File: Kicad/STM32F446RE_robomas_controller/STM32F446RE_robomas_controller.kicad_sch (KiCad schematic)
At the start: 5 parts, among them U3 NUCLEO-F446RE

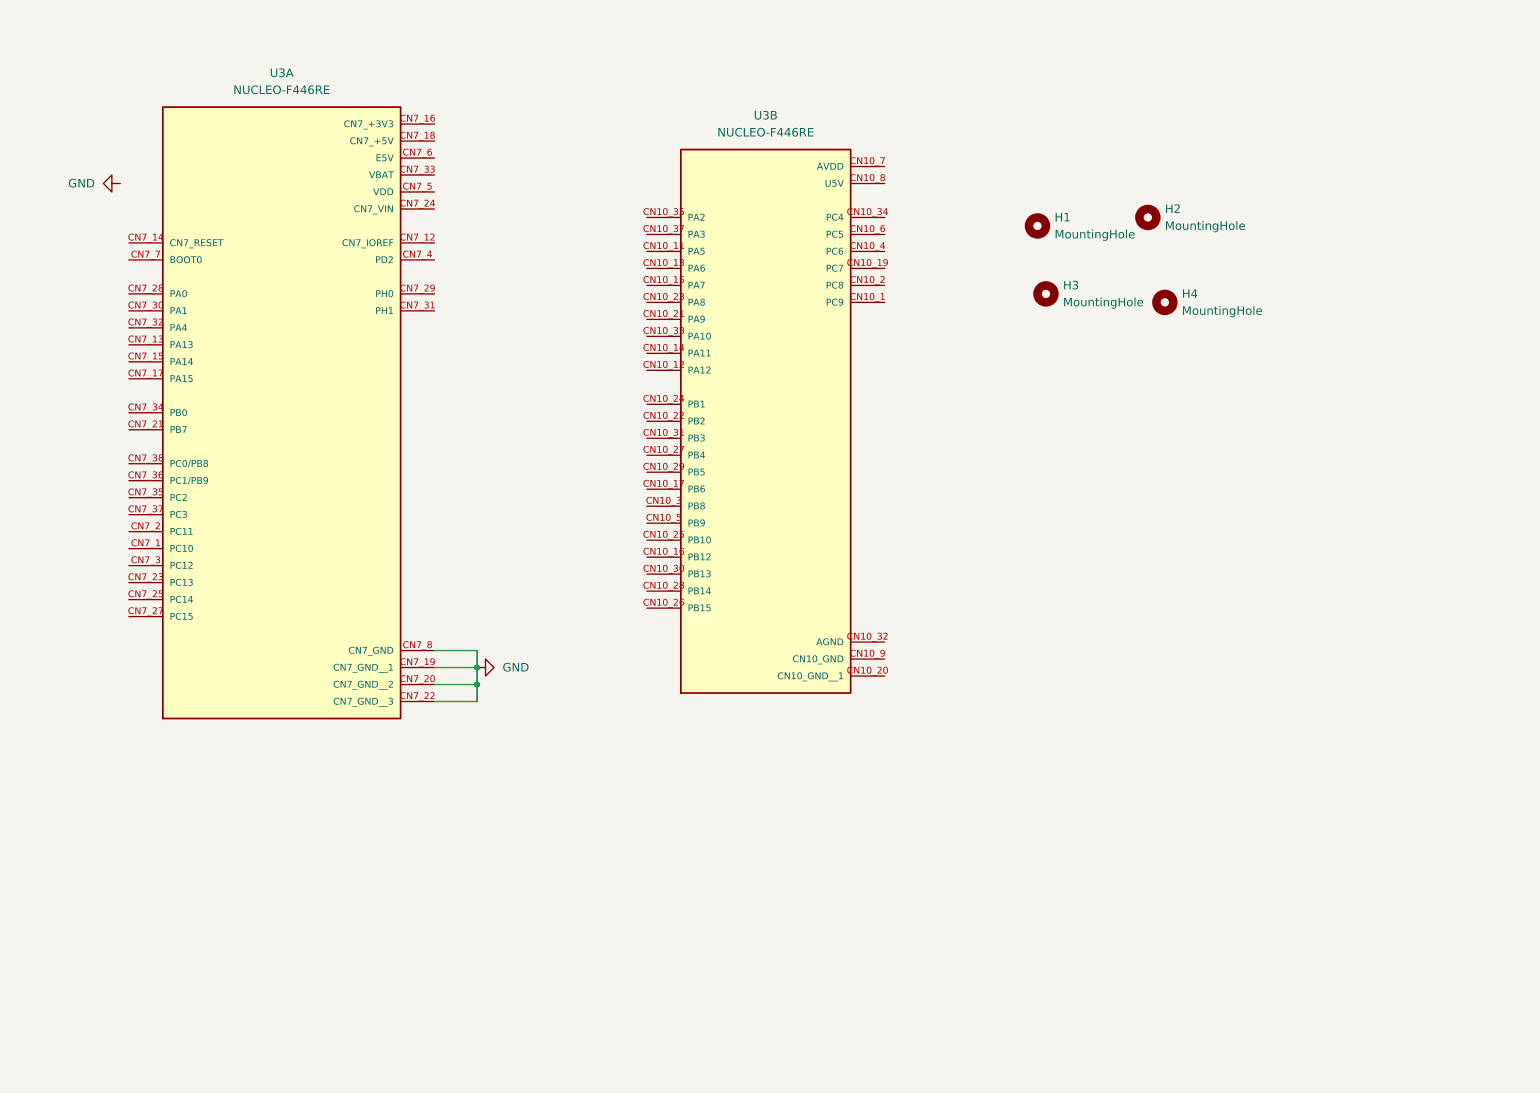
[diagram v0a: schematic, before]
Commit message: robomas用の回路完成
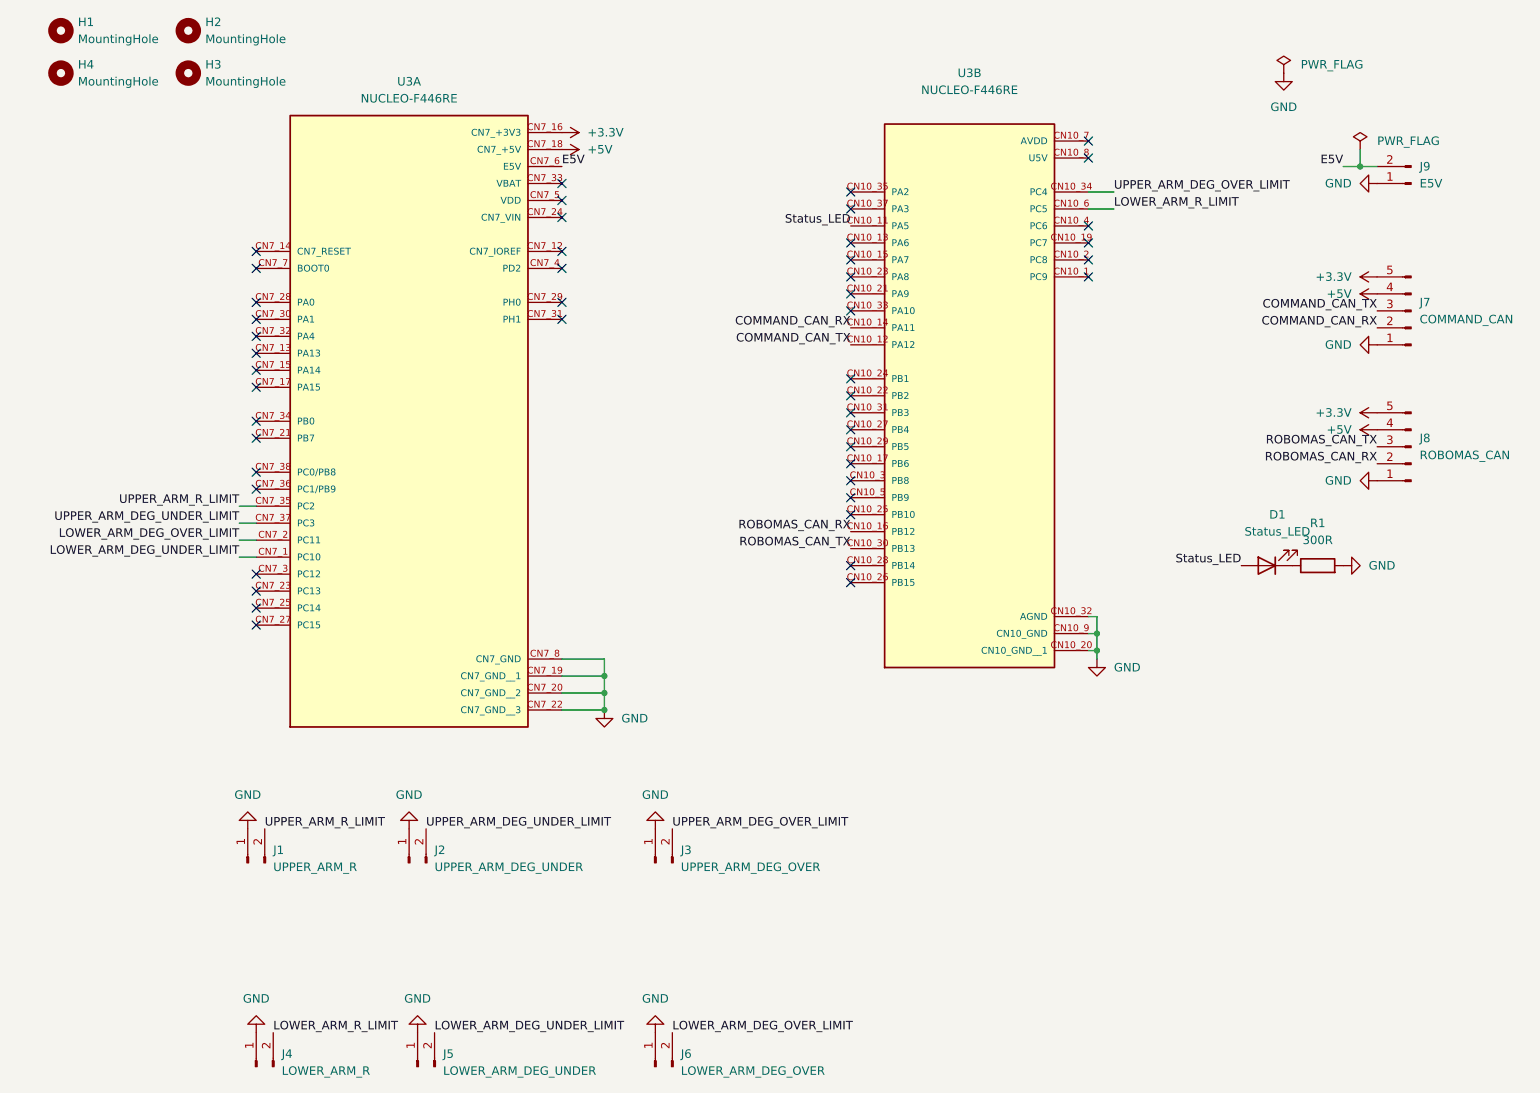
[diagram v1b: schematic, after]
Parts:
- added D1: Status_LED, LED_THT:LED_D3.0mm, symbol Device:LED
- added J1: UPPER_ARM_R, Connector_PinHeader_2.54mm:PinHeader_1x02_P2.54mm_Vertical, symbol Connector:Conn_01x02_Pin
- added J2: UPPER_ARM_DEG_UNDER, Connector_PinHeader_2.54mm:PinHeader_1x02_P2.54mm_Vertical, symbol Connector:Conn_01x02_Pin
- added J3: UPPER_ARM_DEG_OVER, Connector_PinHeader_2.54mm:PinHeader_1x02_P2.54mm_Vertical, symbol Connector:Conn_01x02_Pin
- added J4: LOWER_ARM_R, Connector_PinHeader_2.54mm:PinHeader_1x02_P2.54mm_Vertical, symbol Connector:Conn_01x02_Pin
- added J5: LOWER_ARM_DEG_UNDER, Connector_PinHeader_2.54mm:PinHeader_1x02_P2.54mm_Vertical, symbol Connector:Conn_01x02_Pin
- added J6: LOWER_ARM_DEG_OVER, Connector_PinHeader_2.54mm:PinHeader_1x02_P2.54mm_Vertical, symbol Connector:Conn_01x02_Pin
- added J7: COMMAND_CAN, Connector_PinHeader_2.54mm:PinHeader_1x05_P2.54mm_Vertical, symbol Connector:Conn_01x05_Pin
- added J8: ROBOMAS_CAN, Connector_PinHeader_2.54mm:PinHeader_1x05_P2.54mm_Vertical, symbol Connector:Conn_01x05_Pin
- added J9: E5V, Connector_PinHeader_2.54mm:PinHeader_1x02_P2.54mm_Vertical, symbol Connector:Conn_01x02_Pin
- added R1: 300R, Resistor_THT:R_Axial_DIN0207_L6.3mm_D2.5mm_P7.62mm_Horizontal, symbol Device:R
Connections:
- net GND: now also U3.CN10_20 (CN10_GND__1), U3.CN10_32 (AGND), U3.CN10_9 (CN10_GND), J1.1 (Pin_1), J2.1 (Pin_1), J3.1 (Pin_1), J4.1 (Pin_1), J5.1 (Pin_1), J6.1 (Pin_1), J7.1 (Pin_1), J8.1 (Pin_1), J9.1 (Pin_1), R1.2
- net Status_LED: now reaches U3.CN10_11 (PA5)
- net Status_LED: now also D1.2 (A)
- net COMMAND_CAN_TX: now reaches U3.CN10_12 (PA12)
- net COMMAND_CAN_TX: now also J7.3 (Pin_3)
- net COMMAND_CAN_RX: now reaches U3.CN10_14 (PA11)
- net COMMAND_CAN_RX: now also J7.2 (Pin_2)
- net ROBOMAS_CAN_RX: now reaches U3.CN10_16 (PB12)
- net ROBOMAS_CAN_RX: now also J8.2 (Pin_2)
- net ROBOMAS_CAN_TX: now reaches U3.CN10_30 (PB13)
- net ROBOMAS_CAN_TX: now also J8.3 (Pin_3)
- net UPPER_ARM_DEG_OVER_LIMIT: now reaches U3.CN10_34 (PC4)
- net UPPER_ARM_DEG_OVER_LIMIT: now also J3.2 (Pin_2)
- net LOWER_ARM_R_LIMIT: now reaches U3.CN10_6 (PC5)
- net LOWER_ARM_R_LIMIT: now also J4.2 (Pin_2)
- net LOWER_ARM_DEG_UNDER_LIMIT: now reaches U3.CN7_1 (PC10)
- net LOWER_ARM_DEG_UNDER_LIMIT: now also J5.2 (Pin_2)
- net +3.3V: now reaches U3.CN7_16 (CN7_+3V3)
- net +3.3V: now also J7.5 (Pin_5), J8.5 (Pin_5)
- net +5V: now reaches U3.CN7_18 (CN7_+5V)
- net +5V: now also J7.4 (Pin_4), J8.4 (Pin_4)
- net LOWER_ARM_DEG_OVER_LIMIT: now reaches U3.CN7_2 (PC11)
- net LOWER_ARM_DEG_OVER_LIMIT: now also J6.2 (Pin_2)
- net UPPER_ARM_R_LIMIT: now reaches U3.CN7_35 (PC2)
- net UPPER_ARM_R_LIMIT: now also J1.2 (Pin_2)
- net UPPER_ARM_DEG_UNDER_LIMIT: now reaches U3.CN7_37 (PC3)
- net UPPER_ARM_DEG_UNDER_LIMIT: now also J2.2 (Pin_2)
- net E5V: now reaches U3.CN7_6 (E5V)
- net E5V: now also J9.2 (Pin_2)
- new net: D1.1 (K), R1.1
- no-connect marks 0 -> 47
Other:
- moved on the sheet: H1, H2, H3, H4, U3A, U3B
